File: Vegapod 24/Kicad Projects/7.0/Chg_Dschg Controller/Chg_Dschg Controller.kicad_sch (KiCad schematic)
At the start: 101 parts, among them J1 Slave socket, J10 Boost OUT, J2 Electronics, J3 Charger, J4 Battery, J5 Contactor, J6 NO/NC Contactor, J7 NC/NO Charge, J8 NO/NC Charge-, J9 NO/NC Charge+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

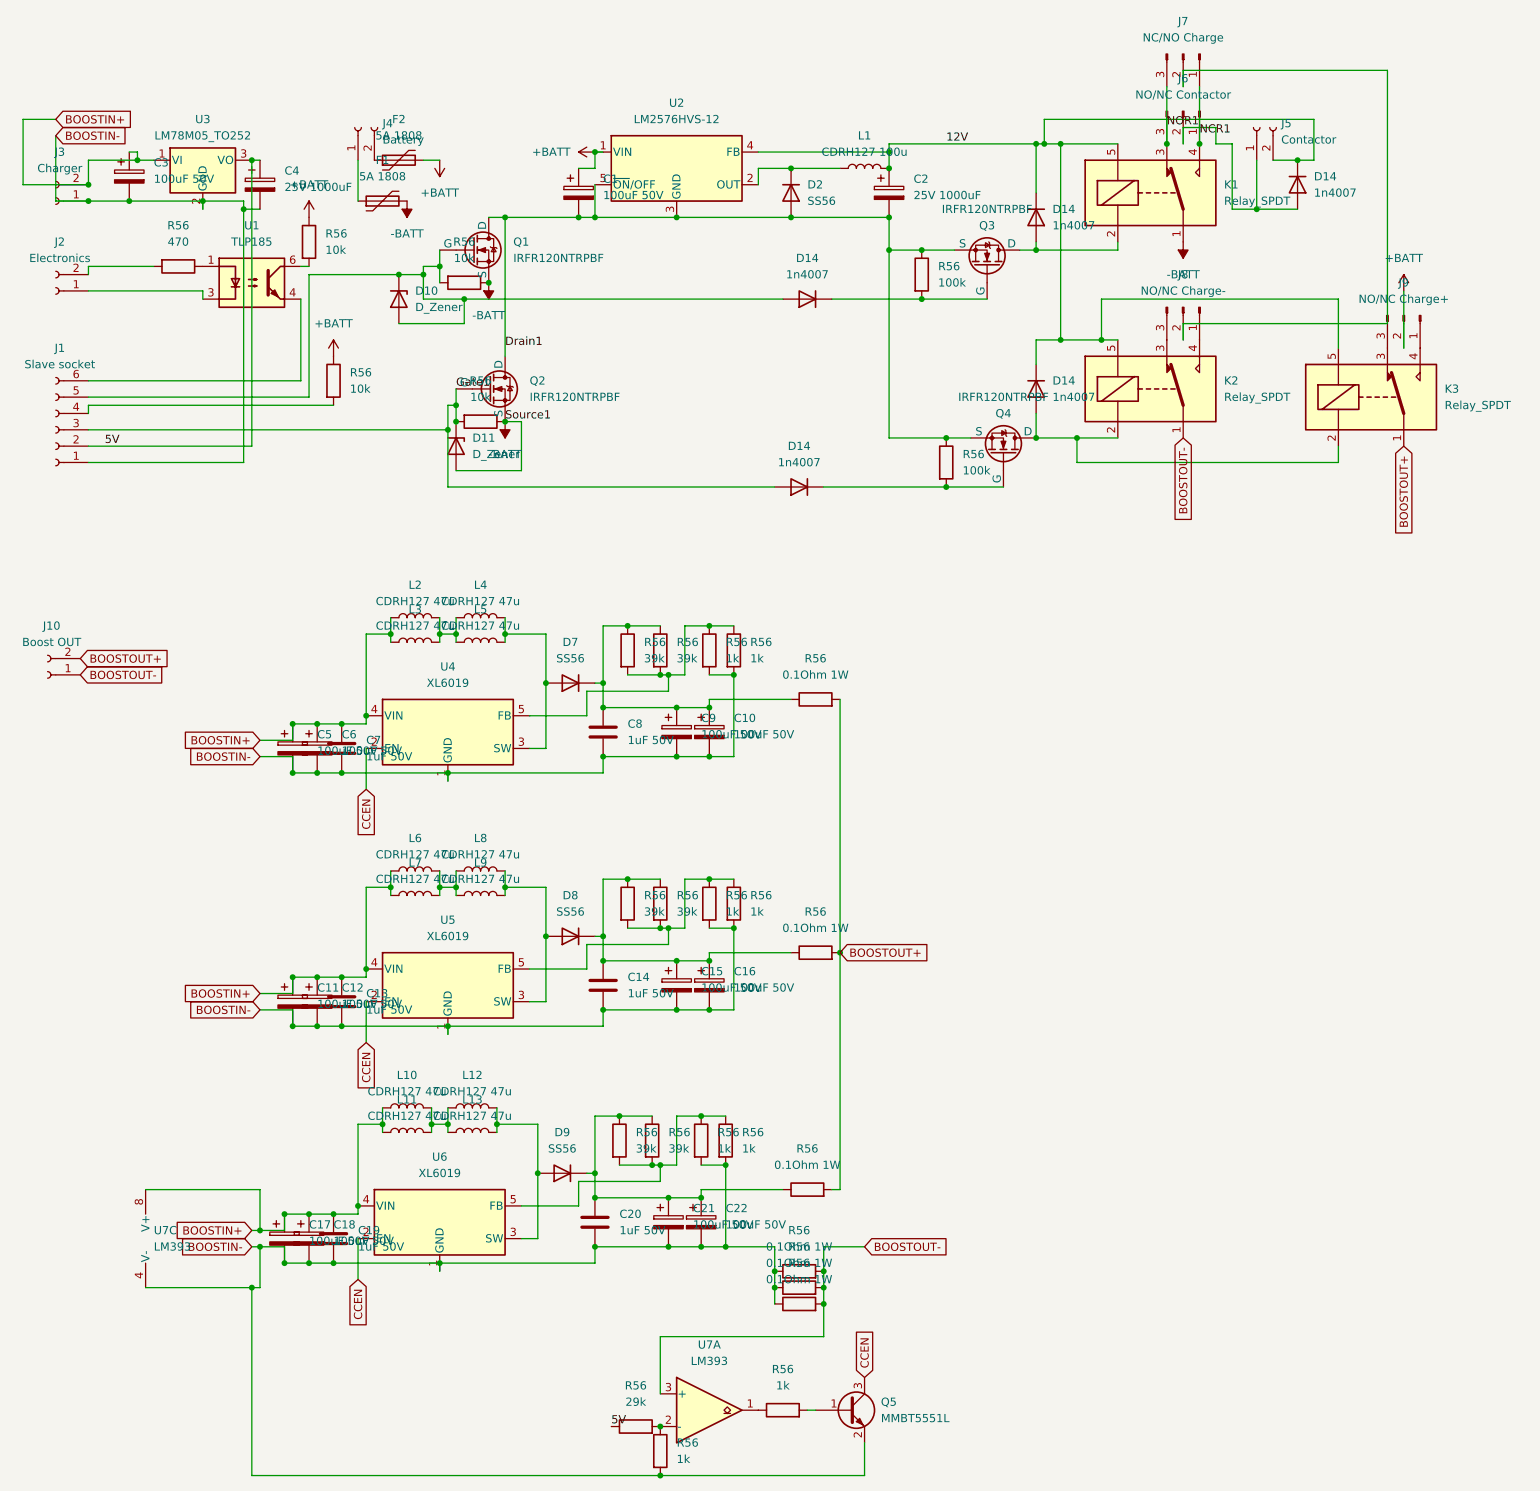
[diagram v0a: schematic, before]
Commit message: Seperated boost converter and chg dschg controller
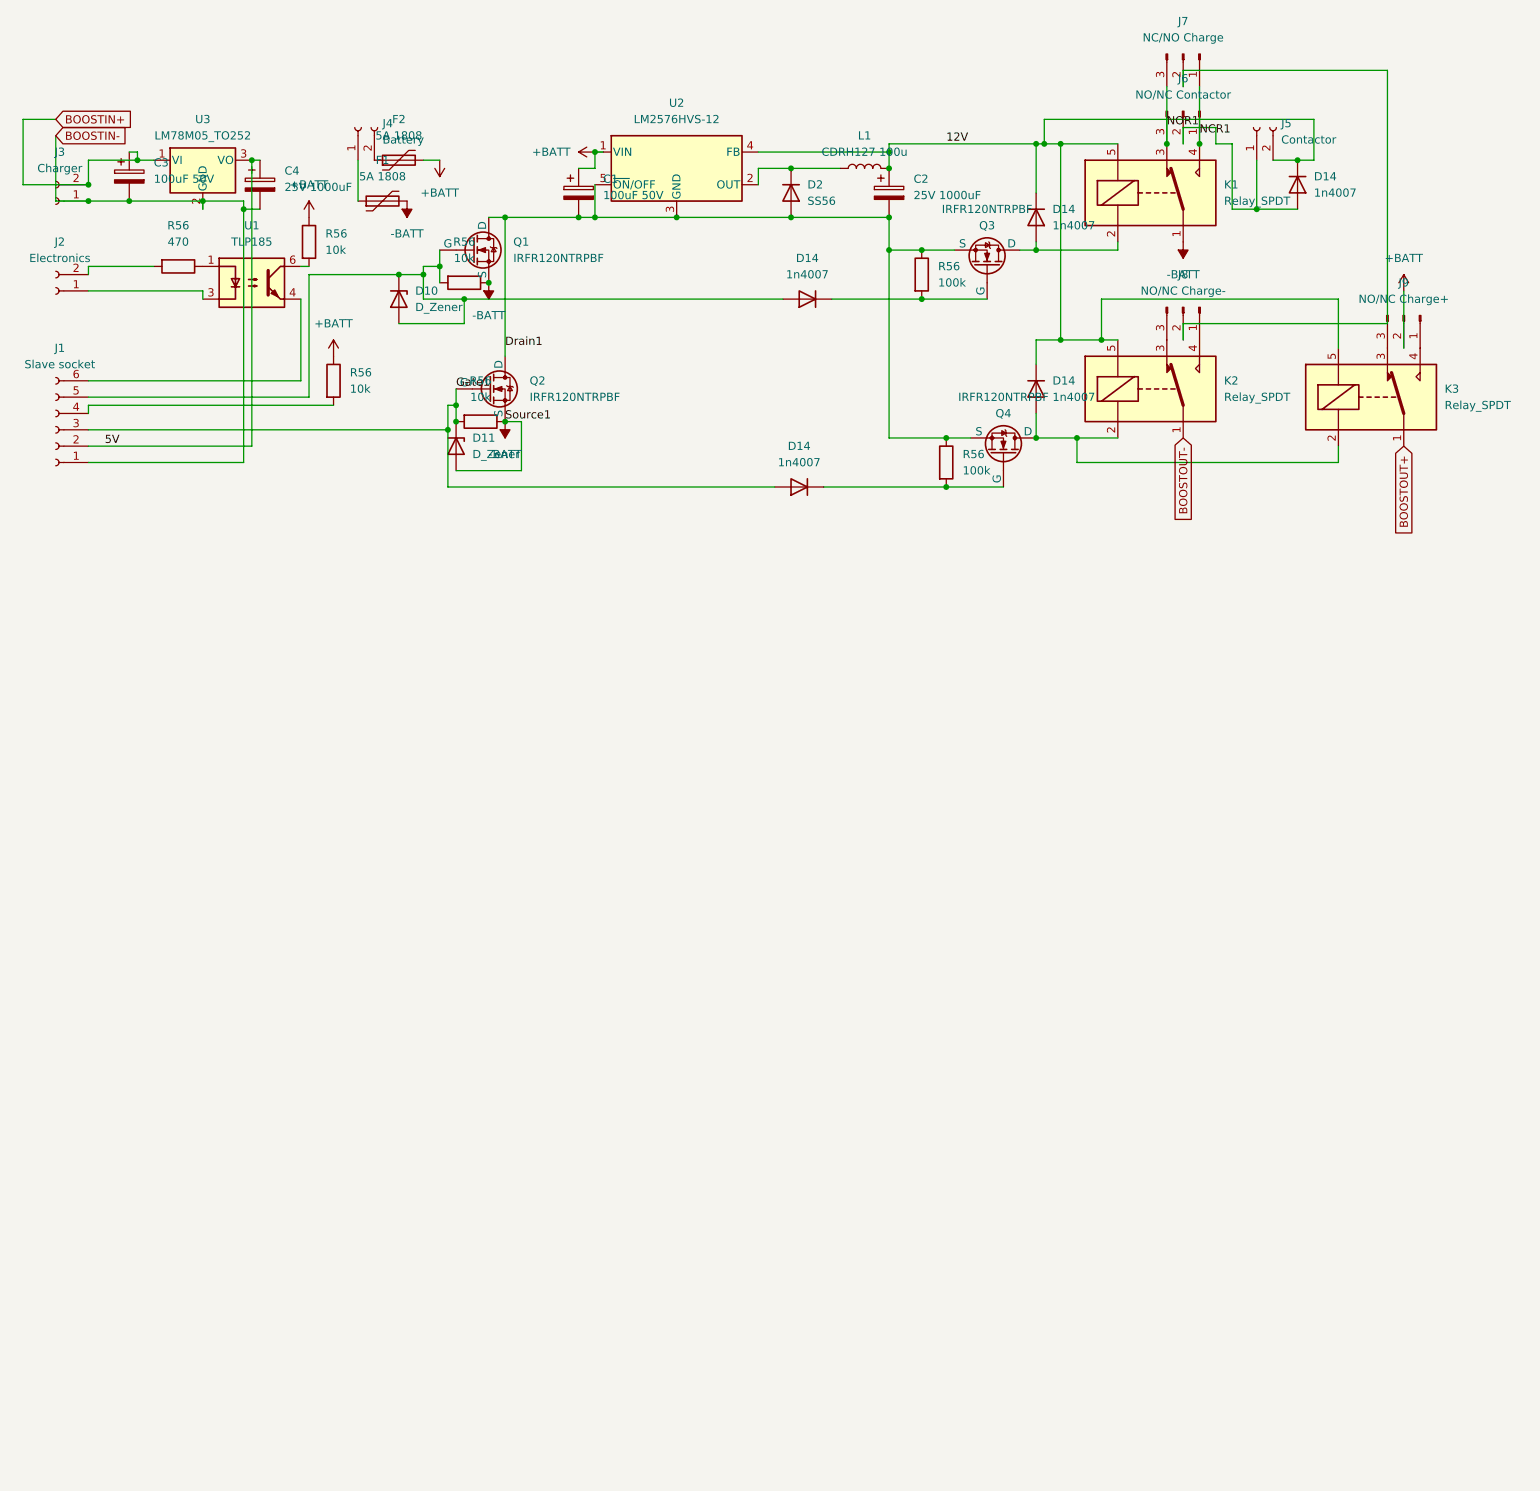
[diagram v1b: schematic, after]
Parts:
- removed C10, C11, C12, C15, C16, C17, C18, C21, C22, C5, C6, C9: 100uF 50V, Capacitor_SMD:CP_Elec_8x10.5, symbol Device:C_Polarized
- removed C13, C14, C19, C20, C7, C8: 1uF 50V, Capacitor_SMD:C_0805_2012Metric_Pad1.18x1.45mm_HandSolder, symbol Device:C
- removed D7, D8, D9: SS56, Diode_SMD:D_SMC, symbol Device:D
- removed J10: Boost OUT, Connector_Phoenix_MC_HighVoltage:PhoenixContact_MCV_1,5_2-G-5.08_1x02_P5.08mm_Vertical, symbol Connector:Conn_01x02_Socket
- removed L10, L11, L12, L13, L2, L3, L4, L5, L6, L7, L8, L9: CDRH127 47u, Inductor_SMD:L_12x12mm_H8mm, symbol Device:L
- removed Q5: MMBT5551L, Package_TO_SOT_SMD:SOT-23, symbol Transistor_BJT:MMBT5551L
- removed R56 (x6): 0.1Ohm 1W, Resistor_SMD:R_2512_6332Metric_Pad1.40x3.35mm_HandSolder, symbol Device:R
- removed R56 (x8): 1k, Resistor_SMD:R_0805_2012Metric_Pad1.20x1.40mm_HandSolder, symbol Device:R
- removed R56 (x6): 39k, Resistor_SMD:R_0805_2012Metric_Pad1.20x1.40mm_HandSolder, symbol Device:R
- removed R56: 29k, Resistor_SMD:R_0805_2012Metric_Pad1.20x1.40mm_HandSolder, symbol Device:R
- removed U4, U5, U6: XL6019, Package_TO_SOT_SMD:TO-263-5_TabPin3, symbol Regulator_Switching:LM2576HVS-12
- removed U7: LM393, Package_SO:SOIC-8-1EP_3.9x4.9mm_P1.27mm_EP2.29x3mm, symbol Comparator:LM393

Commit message: Design of Chg Dschg controller ready
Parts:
- removed C3: 100uF 50V, Capacitor_SMD:CP_Elec_8x10.5, symbol Device:C_Polarized
- removed C4: 25V 1000uF, 25V 1000uF:CAP_EEEFK1E102AQ, symbol Device:C_Polarized
- removed Q1, Q2, Q3, Q4: IRFR120NTRPBF, Package_TO_SOT_SMD:TO-252-2, symbol Simulation_SPICE:NMOS
- added C3, C4, C5: 1uF, Capacitor_SMD:C_1206_3216Metric_Pad1.33x1.80mm_HandSolder, symbol Device:C
- added H1, H2, H3, H4: MountingHole, MountingHole:MountingHole_3.2mm_M3, symbol Mechanical:MountingHole
- added J10: Conn_01x04_Pin, Connector_Phoenix_MC_HighVoltage:PhoenixContact_MCV_1,5_4-G-5.08_1x04_P5.08mm_Vertical, symbol Connector:Conn_01x04_Pin
- added Q1, Q2, Q3, Q5: IRLZ44N, Package_TO_SOT_THT:TO-220-3_Vertical, symbol Transistor_FET:IRLZ44N
- D2: footprint Diode_SMD:D_SMC -> Diode_SMD:D_SMA-SMB_Universal_Handsoldering
- J6, J7, J8, J9: footprint Connector_PinHeader_1.00mm:PinHeader_1x03_P1.00mm_Vertical -> Connector_PinHeader_2.54mm:PinHeader_1x03_P2.54mm_Vertical
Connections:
- net +BATT: now also C5.1
- net -BATT: now also D10.2 (A), Q1.3 (S), Q5.3 (S)
- net 5V: now also C4.1
- net BOOSTIN+: now also C3.1, J10.2 (Pin_2)
- net BOOSTIN-: now also C3.2, C4.2, J10.1 (Pin_1)
- net BOOSTOUT+: now also J10.4 (Pin_4)
- net BOOSTOUT-: now also J10.3 (Pin_3)
- net at D10.1 (K), D14.2 (A), J1.5 (Pin_5)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: now also Q1.1 (G); no longer D10.2 (A)
- net at D14.1 (K), R56.2: now also Q2.1 (G)
- net at D14.2 (A), K2.2, K3.2: now also Q2.2 (D)
- net at D14.2 (A), K1.2: now also Q3.2 (D)
- net at D14.1 (K), R56.2: now also Q3.1 (G)
- net Drain1: no longer names the net of C1.2, C2.2, D2.2 (A), R56.1, R56.1, U2.3 (GND), U2.5 (~{ON}/OFF)
- net Drain1: now also C5.2, Q1.2 (D), Q2.3 (S), Q3.3 (S), Q5.2 (D)
- net Gate1: no longer names the net of D11.1 (K), D14.2 (A), J1.3 (Pin_3), R56.2
- net Gate1: now also Q5.1 (G)
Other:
- moved on the sheet: C1, C2, D10, D11, D14, D2, F1, F2, J1, J2, J3, J4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

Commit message: Added page info to schematic battery module
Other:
- company: (none) -> Vegapod Hyperloop
- title: (none) -> Logic Circuitry Battery Module
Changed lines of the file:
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@@
 (kicad_sch (version 20230121) (generator eeschema)
   (paper "A4")
+  (title_block
+    (title "Logic Circuitry Battery Module")
+    (date "2024-03-14")
+    (rev "0.1")
+    (company "Vegapod Hyperloop")
+  )
   (junction (at 90.17 83.82) (diameter 0) (color 0 0 0 0)
   )
